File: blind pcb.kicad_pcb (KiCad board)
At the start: 2 copper layers, 73.8 x 59.3 mm, 27 parts, among them J1 Screw_Terminal_01x02, J2 Screw_Terminal_01x02, J3 Screw_Terminal_01x02, J4 Screw_Terminal_01x02, J5 Screw_Terminal_01x02, Q1 AO3400A, Q2 AO3400A, Q3 AO3400A, Q4 AO3400A, SW1 SW_SPDT

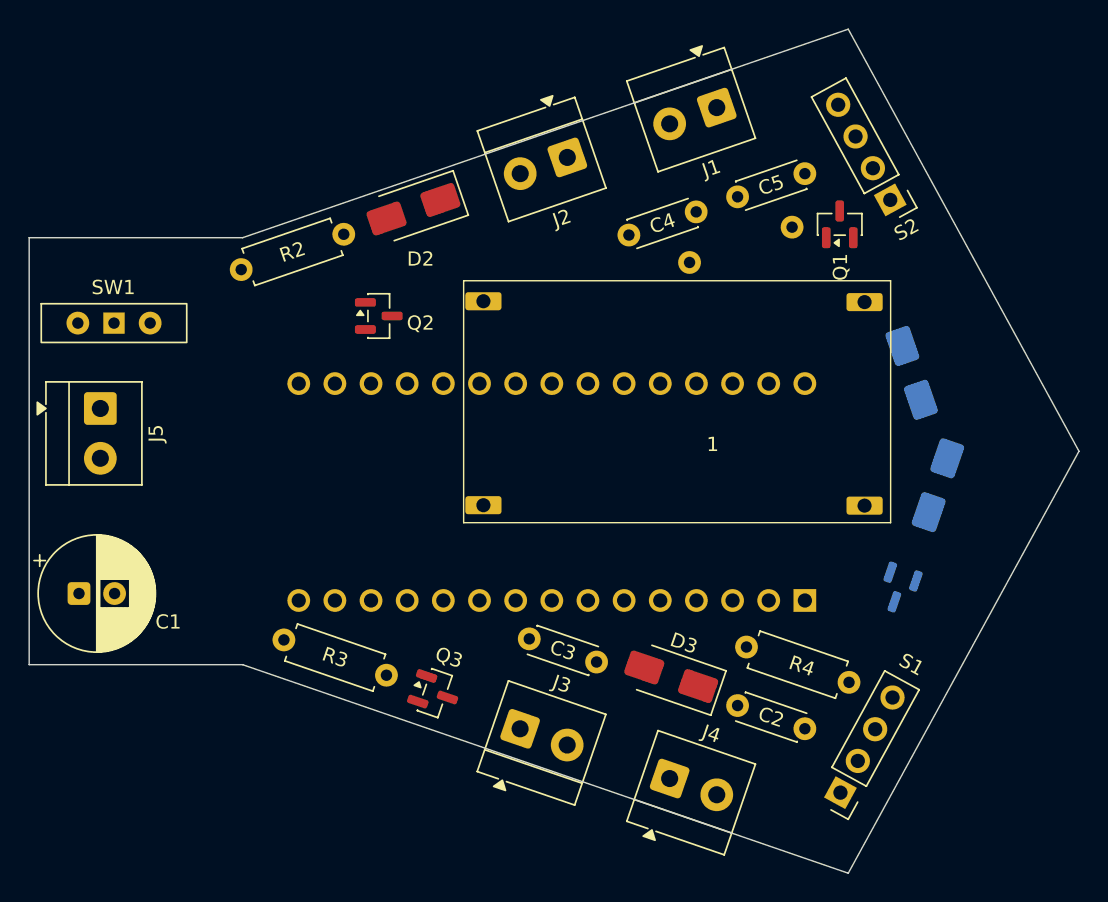
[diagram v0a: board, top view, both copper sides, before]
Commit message: redesign for wider widths of ultrasonic sensors
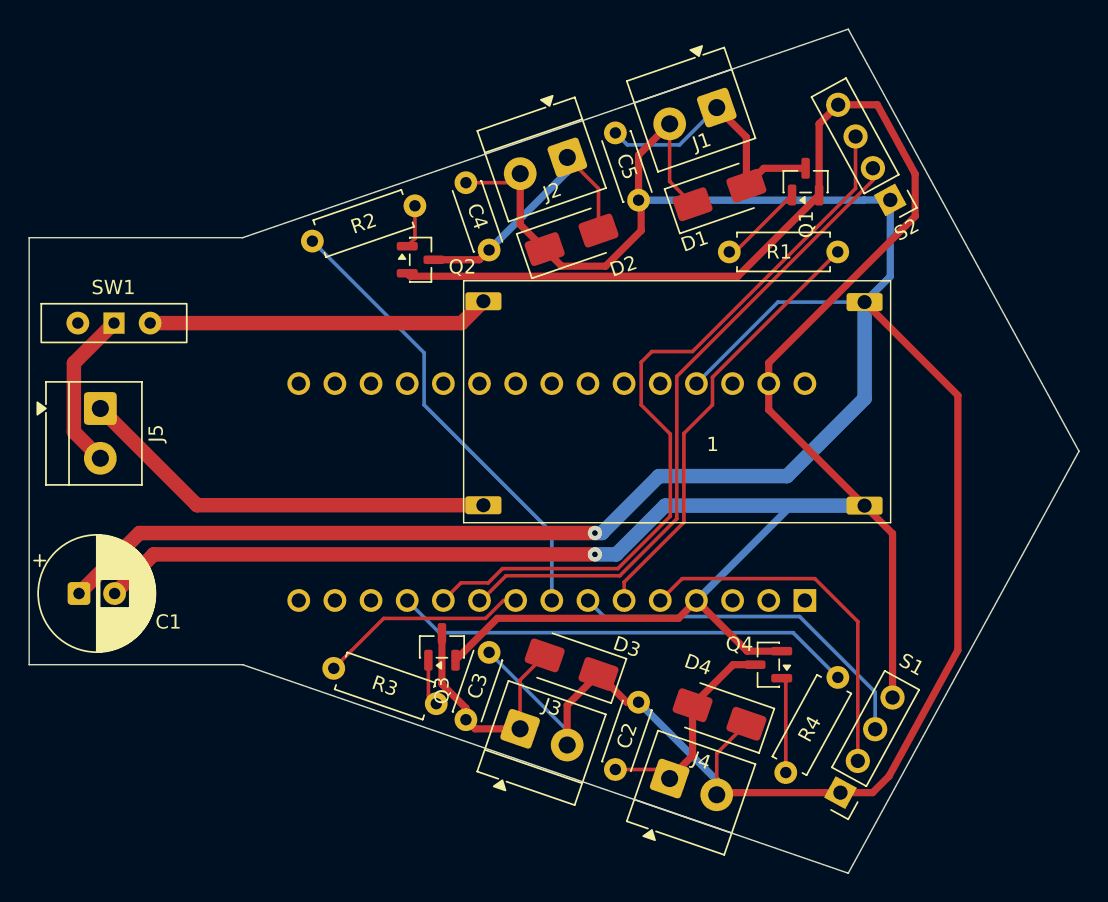
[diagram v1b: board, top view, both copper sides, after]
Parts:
- D1, D4, Q4, R1: moved to F.Cu
- moved D4 22.3 mm to (161.5, 118.5), turned to 161 degrees
- moved D1 18.4 mm to (161.5, 82.0), turned to 19 degrees
- moved R2 13.0 mm to (140.1, 82.8), turned to -161 degrees
- moved C4 12.0 mm to (143.7, 81.1), turned to -71 degrees
- moved C2 11.8 mm to (155.8, 117.6), turned to -109 degrees
- moved D2 11.3 mm to (151.1, 85.2), turned to 19 degrees
- moved Q4 10.6 mm to (164.9, 115.0), turned to 180 degrees
- moved R4 7.74 mm to (166.2, 122.6), turned to 61.301 degrees
- moved C3 7.58 mm to (145.3, 114.1), turned to -109 degrees
- moved D3 7.05 mm to (151.1, 115.0)
- moved C5 6.96 mm to (155.8, 82.4), turned to 109 degrees
- moved Q2 4.92 mm to (140.5, 86.5)
- moved R1 4.74 mm to (162.2, 86.0), turned to 0 degrees
- moved R3 4.03 mm to (141.6, 117.7)
- moved Q1 3.84 mm to (167.6, 81.1)
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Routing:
- net Net-(1-OUT+): track 0.00 -> 223.5 mm, vias 0 -> 1
- net Net-(1-OUT-): track 0.00 -> 187.2 mm, vias 0 -> 1
- net Net-(A1-D8): track 0.00 -> 53.8 mm
- net Net-(A1-D7): track 0.00 -> 46.6 mm
- net Net-(A1-D9): track 0.00 -> 32.5 mm
- net Net-(A1-D5): track 0.00 -> 32.2 mm
- net Net-(A1-D3): track 0.00 -> 30.7 mm
- net Net-(1-IN-): track 0.00 -> 29.7 mm
- net Net-(A1-D2): track 0.00 -> 25.6 mm
- net Net-(A1-D4): track 0.00 -> 25.5 mm
- net Net-(1-IN+): track 0.00 -> 24.1 mm
- net Net-(D1-A): track 0.00 -> 19.6 mm
- net Net-(D2-A): track 0.00 -> 19.0 mm
- net Net-(D3-A): track 0.00 -> 16.7 mm
- net Net-(D4-A): track 0.00 -> 15.5 mm
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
